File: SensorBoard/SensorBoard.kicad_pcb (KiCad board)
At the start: 2 copper layers, 56.1 x 74 mm, 101 parts, among them J1 Conn_01x04_Male, J2 Conn_01x02_Male, U1 JST4Pin, U2 JST4Pin, U3 JST4Pin

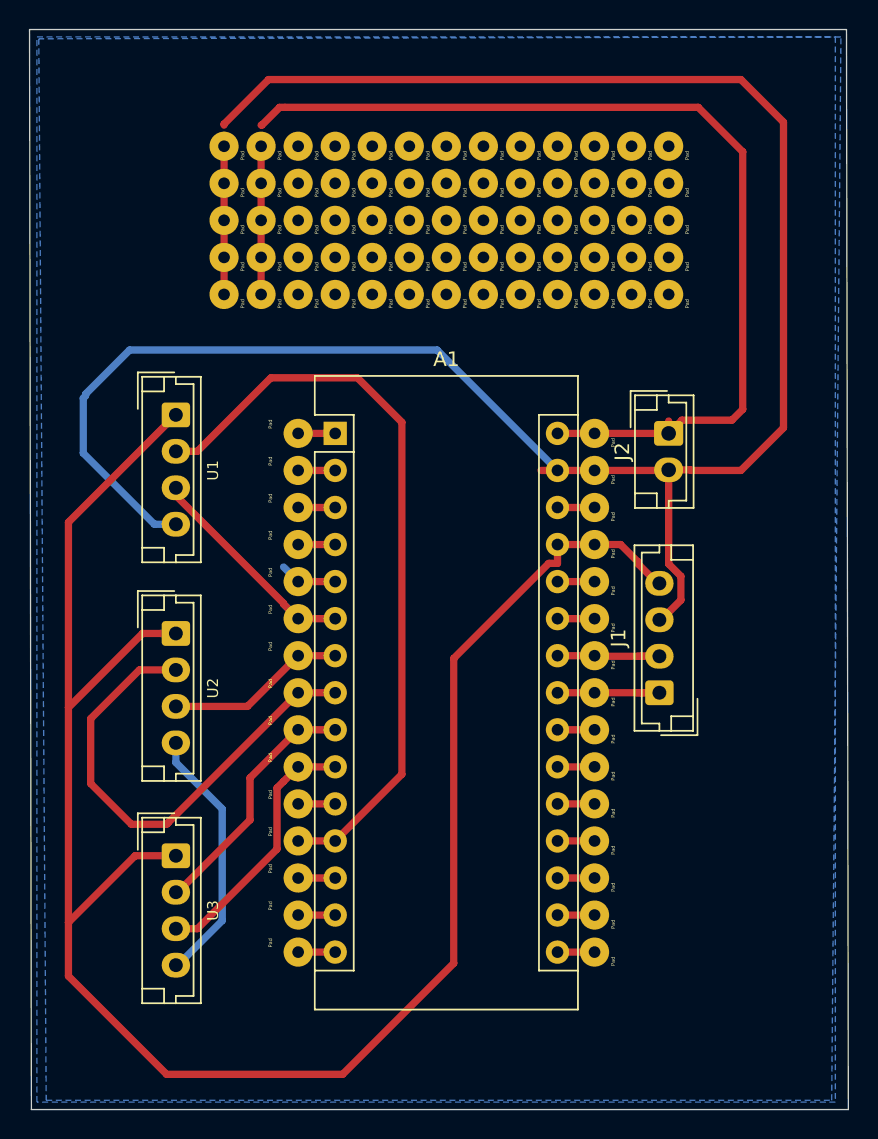
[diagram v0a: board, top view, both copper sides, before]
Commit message: switched pins on ultrasonic to PWM pins and switched some wiring
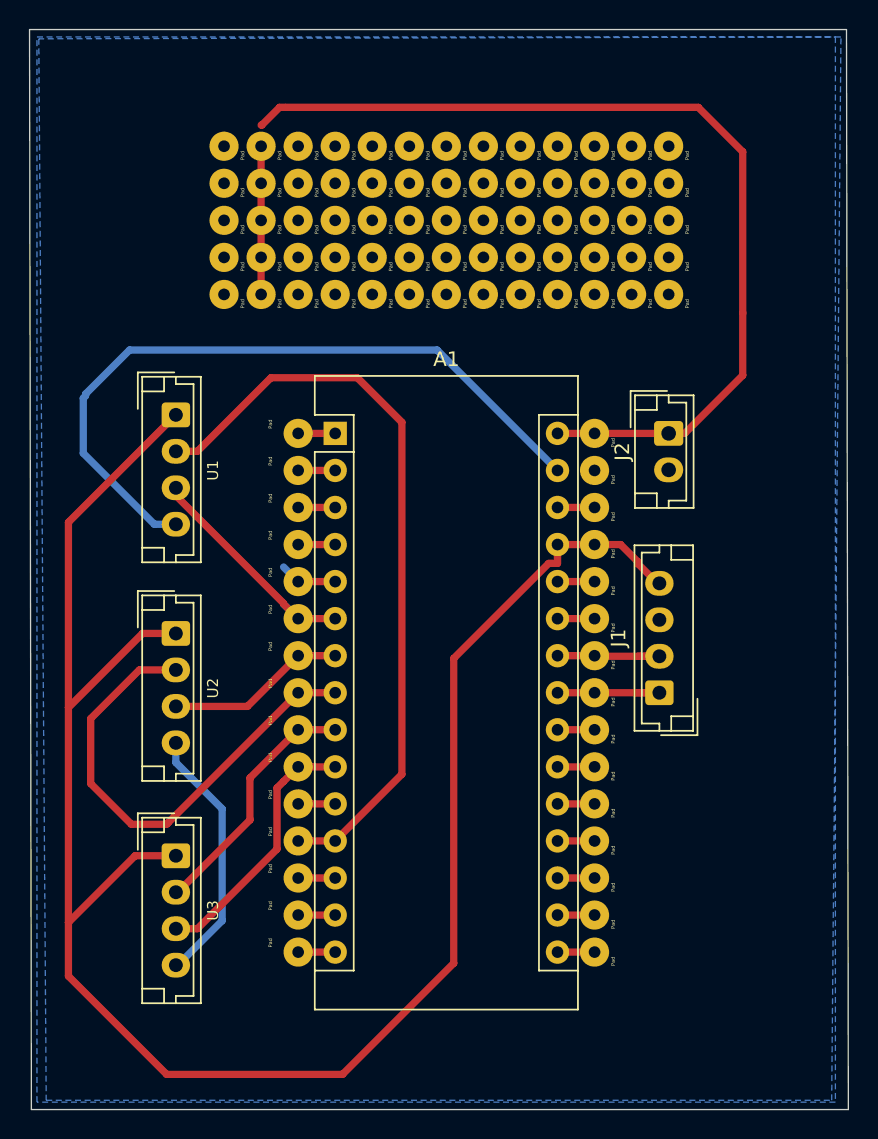
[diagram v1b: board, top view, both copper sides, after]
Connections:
- Pad pad 1: (no net) -> GND (x5)
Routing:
- net GND: track 160.3 -> 68.9 mm
- net (no net): track 21.1 -> 10.2 mm
- net Net-(A1-Pad30): track 66.7 -> 64.5 mm
- net Net-(A1-Pad27): track 133.9 -> 132.8 mm
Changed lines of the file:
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@@
     (thickness 1.6)
     (drawings 4)
-    (tracks 147)
+    (tracks 123)
     (zones 0)
     (modules 101)
@@
   (layers
     (0 F.Cu signal)
-    (31 B.Cu signal)
+    (31 B.Cu signal hide)
     (32 B.Adhes user)
     (33 F.Adhes user)
@@
     (mod_text_size 1 1)
     (mod_text_width 0.15)
-    (pad_size 1.7 1.95)
-    (pad_drill 0.95)
+    (pad_size 1.99898 1.99898)
+    (pad_drill 0.8001)
     (pad_to_mask_clearance 0.051)
     (solder_mask_min_width 0.25)
@@
       (effects (font (size 0.25 0.25) (thickness 0.0625)))
     )
-    (pad 1 thru_hole circle (at 0 0) (size 1.99898 1.99898) (drill 0.8001) (layers *.Cu *.Mask))
+    (pad 1 thru_hole circle (at 0 0) (size 1.99898 1.99898) (drill 0.8001) (layers *.Cu *.Mask)
+      (net 5 GND))
   )
   (module Connector_Wire:SolderWirePad_1x01_Drill0.8mm (layer F.Cu)
@@
     (fp_line (start 1.5 1.5) (end 1.5 -1.5) (layer F.CrtYd) (width 0.05))
     (fp_line (start 1.5 1.5) (end -1.5 1.5) (layer F.CrtYd) (width 0.05))
-    (pad 1 thru_hole circle (at 0 0) (size 1.99898 1.99898) (drill 0.8001) (layers *.Cu *.Mask))
+    (pad 1 thru_hole circle (at 0 0) (size 1.99898 1.99898) (drill 0.8001) (layers *.Cu *.Mask)
+      (net 5 GND))
   )
   (module Connector_Wire:SolderWirePad_1x01_Drill0.8mm (layer F.Cu)
@@
       (effects (font (size 0.25 0.25) (thickness 0.0625)))
     )
-    (pad 1 thru_hole circle (at 0 0) (size 1.99898 1.99898) (drill 0.8001) (layers *.Cu *.Mask))
+    (pad 1 thru_hole circle (at 0 0) (size 1.99898 1.99898) (drill 0.8001) (layers *.Cu *.Mask)
+      (net 5 GND))
   )
   (module Connector_Wire:SolderWirePad_1x01_Drill0.8mm (layer F.Cu)
@@
     (fp_line (start 1.5 1.5) (end 1.5 -1.5) (layer F.CrtYd) (width 0.05))
     (fp_line (start 1.5 1.5) (end -1.5 1.5) (layer F.CrtYd) (width 0.05))
-    (pad 1 thru_hole circle (at 0 0) (size 1.99898 1.99898) (drill 0.8001) (layers *.Cu *.Mask))
+    (pad 1 thru_hole circle (at 0 0) (size 1.99898 1.99898) (drill 0.8001) (layers *.Cu *.Mask)
+      (net 5 GND))
   )
   (module Connector_Wire:SolderWirePad_1x01_Drill0.8mm (layer F.Cu)
@@
       (effects (font (size 0.25 0.25) (thickness 0.0625)))
     )
-    (pad 1 thru_hole circle (at 0 0) (size 1.99898 1.99898) (drill 0.8001) (layers *.Cu *.Mask))
+    (pad 1 thru_hole circle (at 0 0) (size 1.99898 1.99898) (drill 0.8001) (layers *.Cu *.Mask)
+      (net 5 GND))
   )
   (module Connector_Wire:SolderWirePad_1x01_Drill0.8mm (layer F.Cu)
@@
   (gr_line (start 122.682 127.635) (end 178.689 127.635) (layer Edge.Cuts) (width 0.05))
   (gr_line (start 122.555 53.594) (end 122.682 127.635) (layer Edge.Cuts) (width 0.05))
-  (segment (start 135.89 61.595) (end 135.89 64.135) (width 0.5) (layer F.Cu) (net 0))
-  (segment (start 135.89 64.135) (end 135.89 66.675) (width 0.5) (layer F.Cu) (net 0))
-  (segment (start 135.89 66.675) (end 135.89 69.215) (width 0.5) (layer F.Cu) (net 0))
-  (segment (start 135.89 69.215) (end 135.89 71.755) (width 0.5) (layer F.Cu) (net 0))
   (segment (start 138.43 61.595) (end 138.43 64.135) (width 0.5) (layer F.Cu) (net 0))
   (segment (start 138.43 64.135) (end 138.43 66.675) (width 0.5) (layer F.Cu) (net 0))
   (segment (start 138.43 66.675) (end 138.43 69.215) (width 0.5) (layer F.Cu) (net 0))
   (segment (start 138.43 69.215) (end 138.43 71.755) (width 0.5) (layer F.Cu) (net 0))
-  (segment (start 135.89 60.845519) (end 135.89 61.595) (width 0.5) (layer F.Cu) (net 0))
+  (segment (start 135.89 60.845519) (end 135.89 61.595) (width 0.5) (layer F.Cu) (net 5))
   (segment (start 158.75 116.84) (end 161.29 116.84) (width 0.5) (layer F.Cu) (net 1))
   (segment (start 143.51 116.84) (end 140.97 116.84) (width 0.5) (layer F.Cu) (net 2))
   (segment (start 161.29 81.28) (end 158.75 81.28) (width 0.5) (layer F.Cu) (net 3))
-  (segment (start 166.37 81.28) (end 166.37 80.43) (width 0.5) (layer F.Cu) (net 3))
   (segment (start 161.29 81.28) (end 166.37 81.28) (width 0.5) (layer F.Cu) (net 3))
-  (segment (start 167.275553 80.374447) (end 170.704553 80.374447) (width 0.5) (layer F.Cu) (net 3))
-  (segment (start 166.37 81.28) (end 167.275553 80.374447) (width 0.5) (layer F.Cu) (net 3))
-  (segment (start 170.704553 80.374447) (end 171.45 79.629) (width 0.5) (layer F.Cu) (net 3))
-  (segment (start 171.45 79.629) (end 171.45 61.976) (width 0.5) (layer F.Cu) (net 3))
   (segment (start 171.45 61.976) (end 168.402 58.928) (width 0.5) (layer F.Cu) (net 3))
   (segment (start 168.402 58.928) (end 140.081 58.928) (width 0.5) (layer F.Cu) (net 3))
@@
   (segment (start 140.081 58.928) (end 139.7 58.928) (width 0.5) (layer F.Cu) (net 3))
   (segment (start 138.482491 60.145509) (end 138.43 60.145509) (width 0.5) (layer F.Cu) (net 3))
+  (segment (start 171.45 77.3) (end 171.45 73.025) (width 0.5) (layer F.Cu) (net 3))
+  (segment (start 167.47 81.28) (end 171.45 77.3) (width 0.5) (layer F.Cu) (net 3))
+  (segment (start 166.37 81.28) (end 167.47 81.28) (width 0.5) (layer F.Cu) (net 3))
+  (segment (start 171.45 73.025) (end 171.45 61.976) (width 0.5) (layer F.Cu) (net 3))
   (segment (start 140.97 114.3) (end 143.51 114.3) (width 0.5) (layer F.Cu) (net 4))
   (segment (start 166.33 83.82) (end 166.37 83.78) (width 0.5) (layer F.Cu) (net 5))
-  (segment (start 161.29 83.82) (end 166.33 83.82) (width 0.5) (layer F.Cu) (net 5))
-  (segment (start 167.21 91.071509) (end 167.21 92.71) (width 0.5) (layer F.Cu) (net 5))
-  (segment (start 166.37 90.231509) (end 167.21 91.071509) (width 0.5) (layer F.Cu) (net 5))
-  (segment (start 167.21 92.71) (end 165.86 94.06) (width 0.5) (layer F.Cu) (net 5))
-  (segment (start 166.37 83.78) (end 166.37 90.231509) (width 0.5) (layer F.Cu) (net 5))
-  (segment (start 161.29 83.82) (end 158.75 83.82) (width 0.5) (layer F.Cu) (net 5))
-  (segment (start 158.75 83.82) (end 157.61863 83.82) (width 0.5) (layer F.Cu) (net 5))
-  (segment (start 167.62 83.78) (end 167.66 83.82) (width 0.25) (layer F.Cu) (net 5))
-  (segment (start 166.37 83.78) (end 167.62 83.78) (width 0.25) (layer F.Cu) (net 5))
-  (segment (start 167.87 83.78) (end 167.91 83.82) (width 0.5) (layer F.Cu) (net 5))
-  (segment (start 166.37 83.78) (end 167.87 83.78) (width 0.5) (layer F.Cu) (net 5))
-  (segment (start 167.91 83.82) (end 171.323 83.82) (width 0.5) (layer F.Cu) (net 5))
-  (segment (start 171.323 83.82) (end 174.244 80.899) (width 0.5) (layer F.Cu) (net 5))
-  (segment (start 174.244 80.899) (end 174.244 59.944) (width 0.5) (layer F.Cu) (net 5))
-  (segment (start 174.244 59.944) (end 171.323 57.023) (width 0.5) (layer F.Cu) (net 5))
-  (segment (start 138.938 57.023) (end 135.89 60.071) (width 0.5) (layer F.Cu) (net 5))
-  (segment (start 171.323 57.023) (end 138.938 57.023) (width 0.5) (layer F.Cu) (net 5))
   (segment (start 132.588 117.736) (end 132.463 117.736) (width 0.5) (layer F.Cu) (net 5))
   (segment (start 132.588 117.736) (end 132.713 117.736) (width 0.5) (layer F.Cu) (net 5))
@@
   (segment (start 150.495 75.565) (end 158.75 83.82) (width 0.5) (layer B.Cu) (net 5))
   (segment (start 129.413 75.565) (end 150.495 75.565) (width 0.5) (layer B.Cu) (net 5))
-  (segment (start 135.89 60.145509) (end 135.89 60.071) (width 0.5) (layer F.Cu) (net 5))
   (segment (start 132.588 87.51) (end 132.463 87.51) (width 0.5) (layer F.Cu) (net 5))
   (segment (start 132.463 102.496) (end 132.588 102.496) (width 0.5) (layer F.Cu) (net 5))
@@
   (segment (start 164.26 90.085) (end 164.26 90.21) (width 0.5) (layer F.Cu) (net 9))
   (segment (start 161.29 88.9) (end 163.075 88.9) (width 0.5) (layer F.Cu) (net 9))
-  (segment (start 132.588 94.996) (end 131.513 94.996) (width 0.5) (layer B.Cu) (net 9))
   (segment (start 158.149999 90.189999) (end 151.638 96.701998) (width 0.5) (layer F.Cu) (net 9))
   (segment (start 158.75 88.9) (end 158.75 90.189999) (width 0.5) (layer F.Cu) (net 9))
